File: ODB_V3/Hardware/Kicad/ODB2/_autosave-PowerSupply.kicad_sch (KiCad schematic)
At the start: 39 parts, among them U7 MPQ9843GLE-5-AEC1-Z

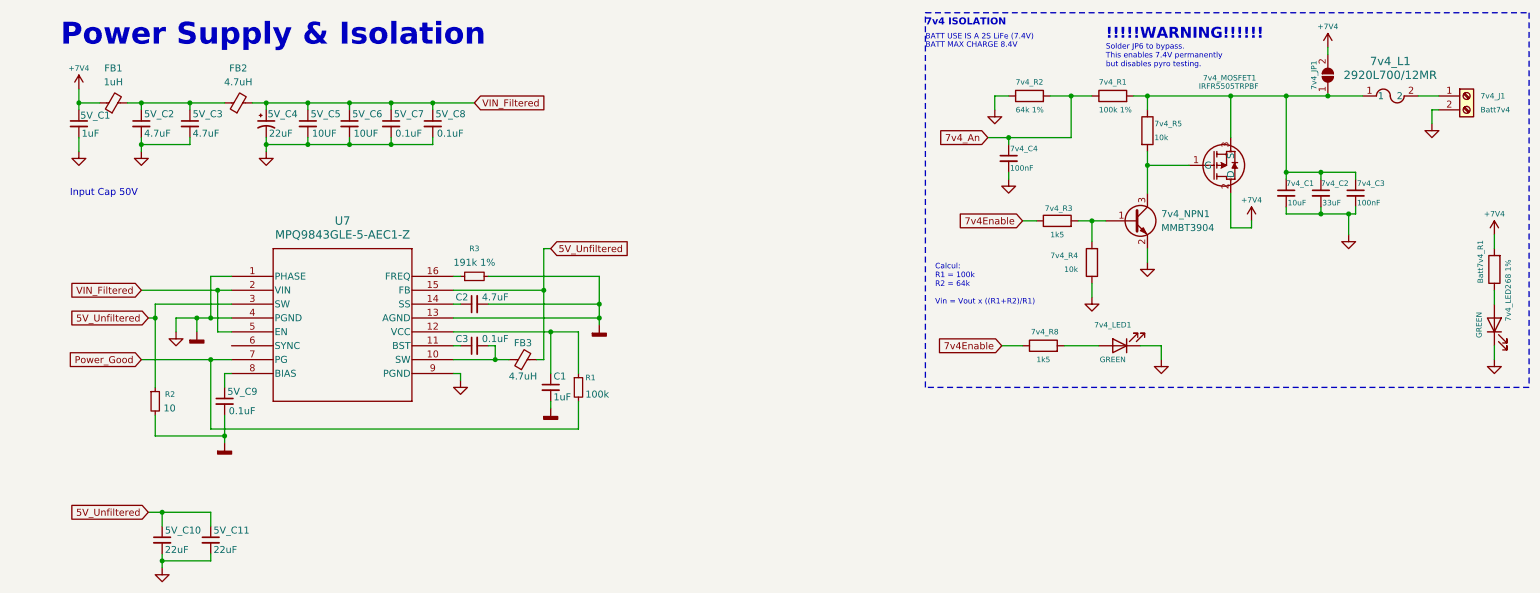
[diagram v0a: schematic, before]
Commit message: feat: new psu design from 5v-36v to 5v (not final)
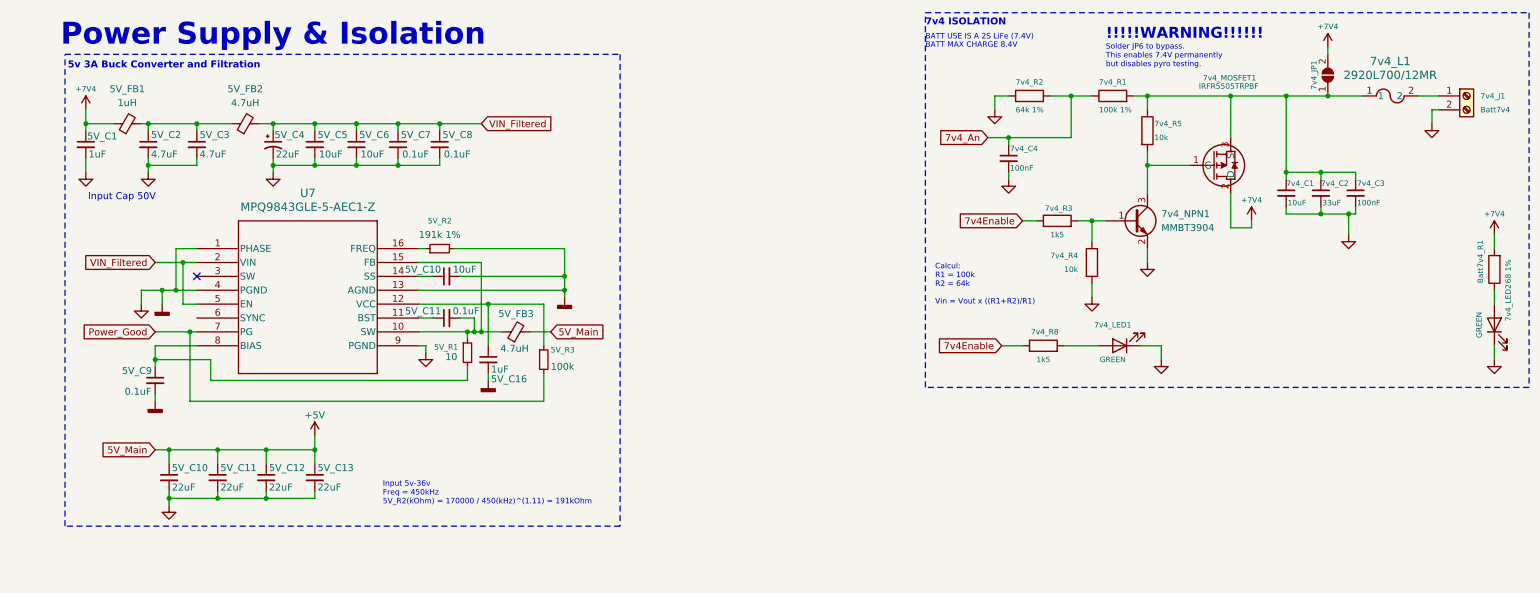
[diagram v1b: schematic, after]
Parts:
- added 5V_C12, 5V_C13: 22uF, Capacitor_SMD:C_1210_3225Metric, symbol Device:C_Small
- 5V_C10: renamed from C2; value 4.7uF -> 10uF
- 5V_C5, 5V_C6: value 10UF -> 10uF
- renumbered C3 to 5V_C11, C1 to 5V_C16, FB1 to 5V_FB1, FB2 to 5V_FB2, FB3 to 5V_FB3, R2 to 5V_R1, R3 to 5V_R2, R1 to 5V_R3
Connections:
- net GND: now also 5V_C12.2, 5V_C13.2; no longer 5V_R1.2
- net at 5V_C11.2, 5V_FB3.1, U7.10 (SW): now also 5V_R1.1, U7.15 (FB)
- net at 5V_C9.1, U7.8 (BIAS): now also 5V_R1.2
- net 5V_Unfiltered renamed +5V
- net +5V: now also 5V_C12.1, 5V_C13.1; no longer 5V_R1.1, U7.15 (FB), U7.3 (SW)
- no-connect marks 0 -> 1
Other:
- note added: "5v 3A Buck Converter and Filtration"
- note added: "Input 5v-36v Freq = 450kHz 5V_R2(kOhm) = 170000 / 450(kHz)^(1.11) = 191kOhm"
- moved on the sheet: 5V_C1, 5V_C10, 5V_C11, 5V_C16, 5V_C2, 5V_C3, 5V_C4, 5V_C5, 5V_C6, 5V_C7, 5V_C8, 5V_C9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
